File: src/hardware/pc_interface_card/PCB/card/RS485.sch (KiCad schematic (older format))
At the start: 13 parts, among them U1 NCP1117-5.0, U2 FT230XQ, U3 THVD1450DR

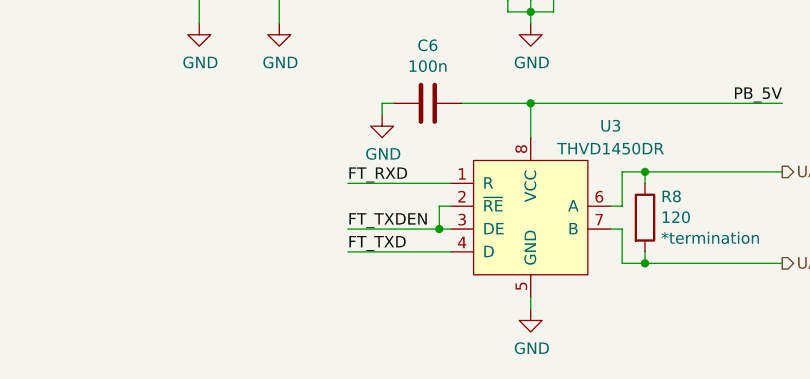
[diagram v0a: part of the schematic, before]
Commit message: Changing ~RE connection in U3 THVD1450DR to GND to always enable receiving from the RS485 bus to better handle error and collision detections Fixing symbol library location
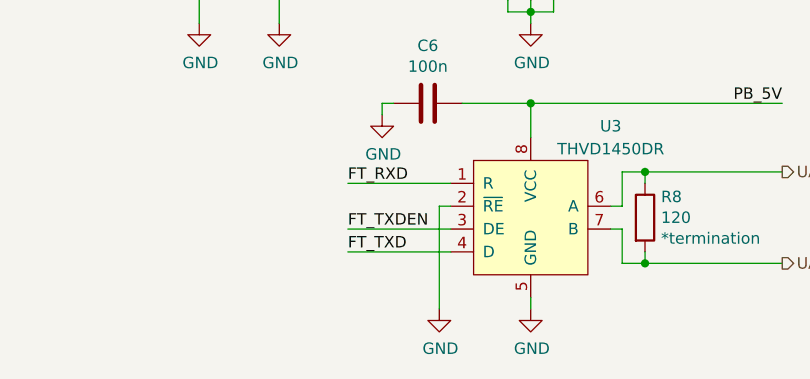
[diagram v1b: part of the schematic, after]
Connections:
- net FT_TXDEN: no longer U3.2 (~RE)
- net GND: now also U3.2 (~RE)
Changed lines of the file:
@@
 Sheet 2 3
 Title "Alpha Card PC Interface"
-Date "2020-04-12"
-Rev "1"
+Date "2020-07-26"
+Rev "2"
 Comp "Halidelabs"
 Comment1 "halidelabs.eu"
@@
 Text Label 5300 5500 0    50   ~ 0
 FT_TXDEN
-Wire Wire Line
-	5300 5500 5700 5500
 $Comp
 L power:GND #PWR?
@@
 Wire Wire Line
 	5750 5400 5700 5400
-Wire Wire Line
-	5700 5400 5700 5500
-Connection ~ 5700 5500
-Wire Wire Line
-	5700 5500 5750 5500
 NoConn ~ 6800 3900
 Wire Wire Line
@@
 Text HLabel 4050 3800 0    50   Input ~ 0
 USB_D+
+Wire Wire Line
+	5300 5500 5750 5500
+$Comp
+L power:GND #PWR?
+U 1 1 5F1F6338
+P 5700 5850
+AR Path="/5F1F6338" Ref="#PWR?"  Part="1"
+AR Path="/5EA5E705/5F1F6338" Ref="#PWR0101"  Part="1"
+F 0 "#PWR0101" H 5700 5600 50  0001 C CNN
+F 1 "GND" H 5705 5677 50  0000 C CNN
+F 2 "" H 5700 5850 50  0001 C CNN
+F 3 "" H 5700 5850 50  0001 C CNN
+	1    5700 5850
+	1    0    0    -1
+$EndComp
+Wire Wire Line
+	5700 5400 5700 5850
 $EndSCHEMATC

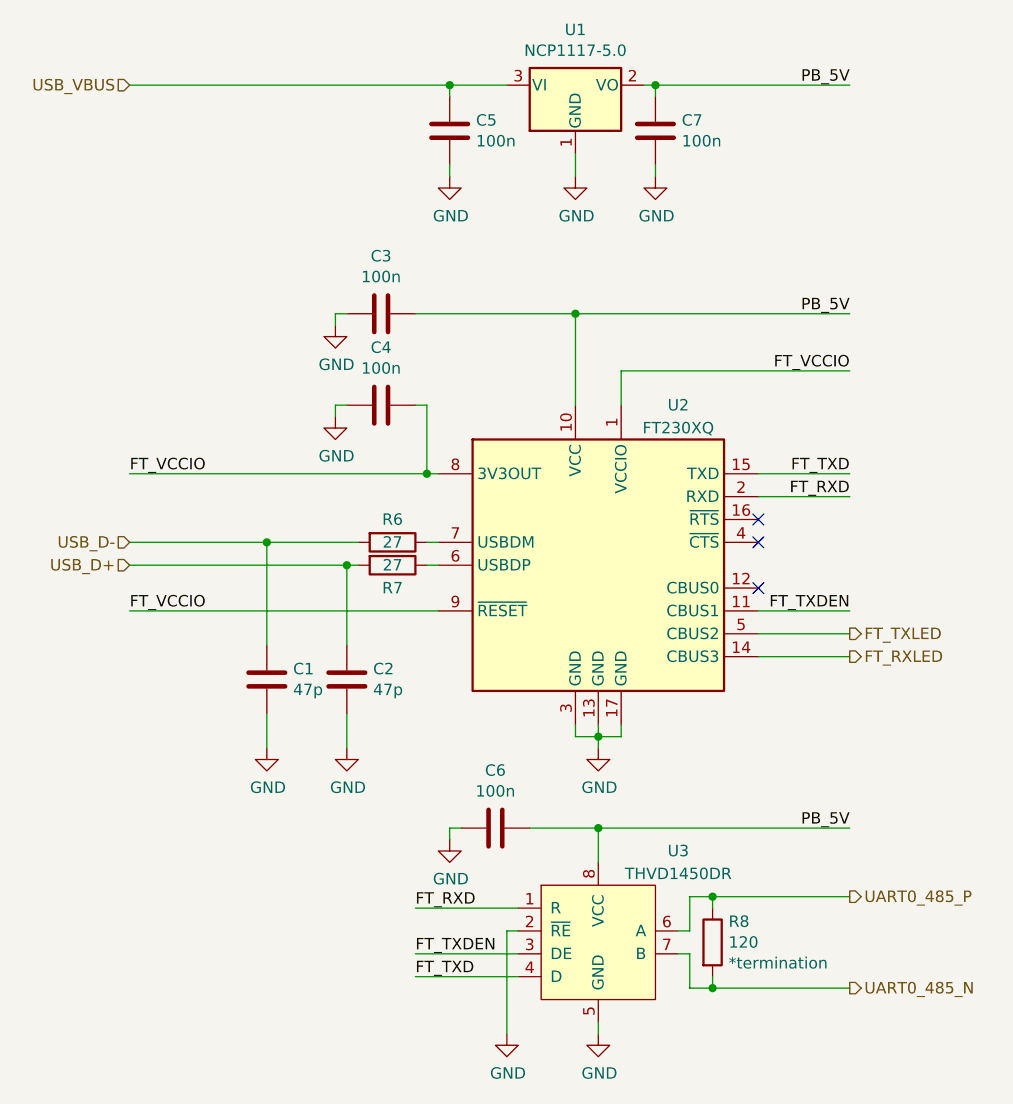
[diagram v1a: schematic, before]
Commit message: Fixing RXLED and TXLED polarization
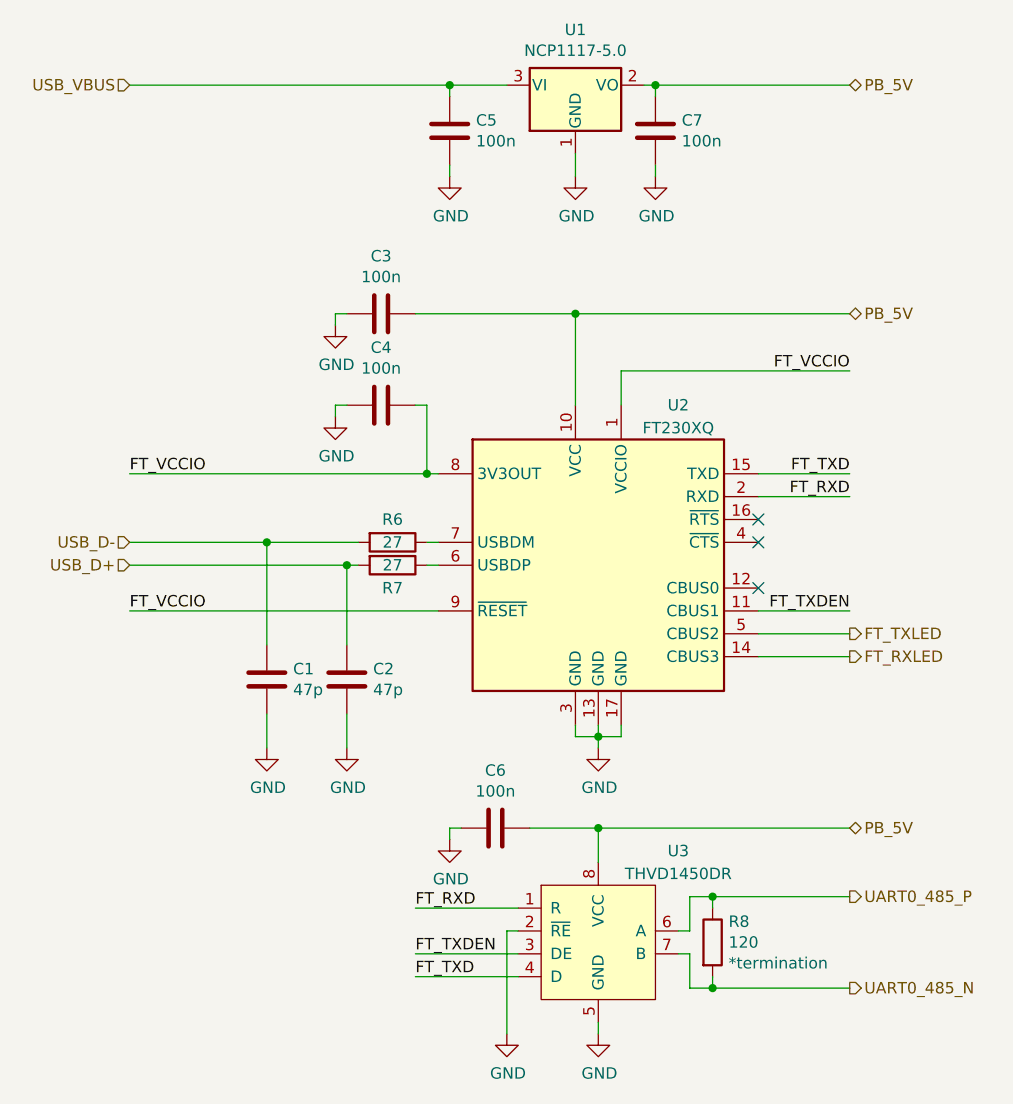
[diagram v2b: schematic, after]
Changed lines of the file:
@@
 Wire Wire Line
 	5450 1700 5450 1750
-Text Label 7200 1700 2    50   ~ 0
-PB_5V
 Wire Wire Line
 	7200 1700 6350 1700
@@
 Wire Wire Line
 	4950 2700 5000 2700
-Text Label 7200 2700 2    50   ~ 0
-PB_5V
 Wire Wire Line
 	7200 2700 6000 2700
@@
 Wire Wire Line
 	6100 4950 6100 5100
-Text Label 7200 4950 2    50   ~ 0
-PB_5V
 Wire Wire Line
 	7200 4950 6100 4950
@@
 Wire Wire Line
 	5700 5400 5700 5850
+Text HLabel 7200 2700 2    50   BiDi ~ 0
+PB_5V
+Text HLabel 7200 1700 2    50   BiDi ~ 0
+PB_5V
+Text HLabel 7200 4950 2    50   BiDi ~ 0
+PB_5V
 $EndSCHEMATC
